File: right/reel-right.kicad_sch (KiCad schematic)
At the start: 42 parts, among them J1 Conn_01x02, SW1 SW_Push, SW10 SW_Push, SW11 SW_Push, SW12 SW_Push, SW13 SW_Push, SW14 SW_Push, SW15 SW_Push, SW16 SW_Push, SW17 SW_Push, SW18 SW_Push, SW19 SW_Push, SW2 SW_Push, SW22 SW_SPDT, SW3 SW_Push, SW4 SW_Push, SW5 SW_Push, SW6 SW_Push, SW7 SW_Push, SW8 SW_Push, SW9 SW_Push, U1 XIAO-nRF52840-Plus-SMD

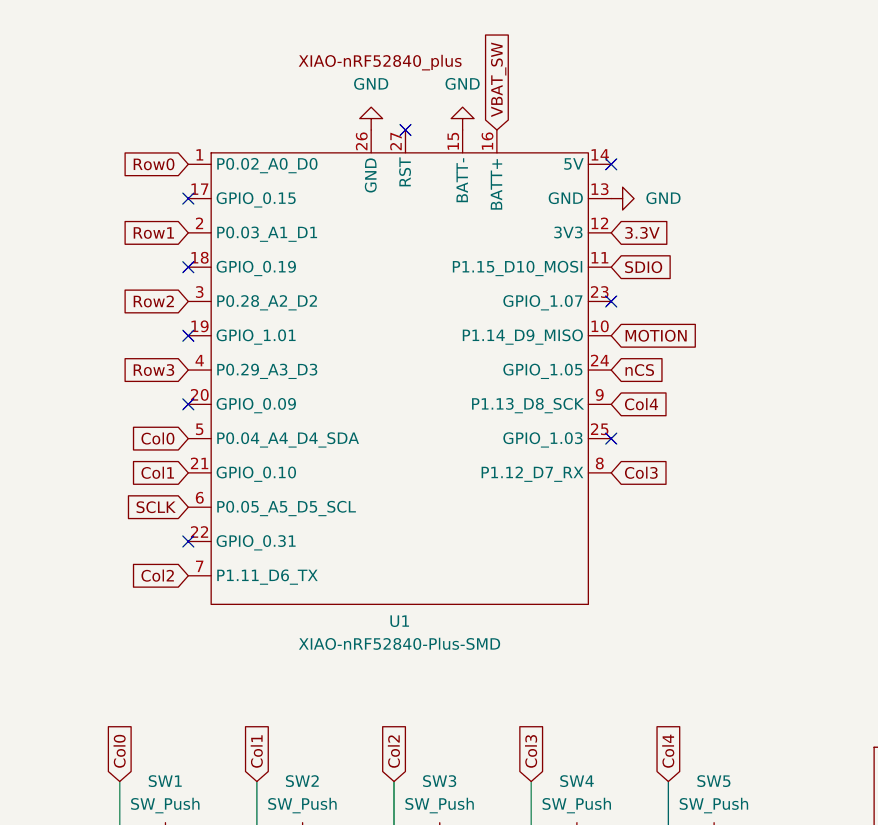
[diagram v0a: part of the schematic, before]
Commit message: Update XIAO BLE footprints
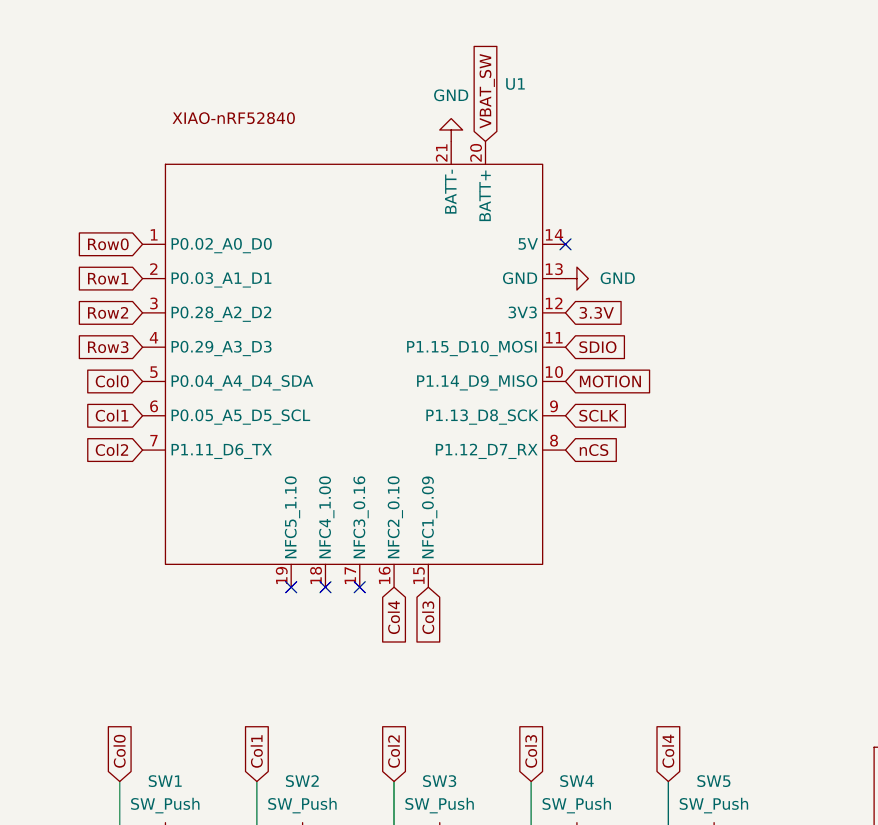
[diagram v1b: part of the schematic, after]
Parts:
- removed U1: XIAO-nRF52840-Plus-SMD, reel:XIAO_nRF52840_plus_mki, symbol smkbd_Library:XIAO-nRF52840_plus_maked_by_mki
- added U1: (no value), reel:XIAO_nRF52840_wBAT_wNFC_1, symbol roba:XIAO-nRF52840
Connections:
- net 3.3V: now also U1.12 (3V3)
- net Col0: now also U1.5 (P0.04_A4_D4_SDA)
- net Col1: now also U1.6 (P0.05_A5_D5_SCL)
- net Col2: now also U1.7 (P1.11_D6_TX)
- net Col3: now also U1.15 (NFC1_0.09)
- net Col4: now also U1.16 (NFC2_0.10)
- net GND: now also U1.13 (GND), U1.21 (BATT-)
- net MOTION: now also U1.10 (P1.14_D9_MISO)
- net Row0: now also U1.1 (P0.02_A0_D0)
- net Row1: now also U1.2 (P0.03_A1_D1)
- net Row2: now also U1.3 (P0.28_A2_D2)
- net Row3: now also U1.4 (P0.29_A3_D3)
- net SCLK: now also U1.9 (P1.13_D8_SCK)
- net SDIO: now also U1.11 (P1.15_D10_MOSI)
- net VBAT_SW: now also U1.20 (BATT+)
- net nCS: now also U1.8 (P1.12_D7_RX)
- no-connect marks 11 -> 6
